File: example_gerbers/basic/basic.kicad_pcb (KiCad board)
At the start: 2 copper layers, 10 x 15 mm, 0 parts

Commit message: Updated basic example
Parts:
- added SP1: Simulation-Port, antmicro-footprints:Simulation-Port, F.Cu at (143.0, 103.3)
- added SP2: Simulation-Port, antmicro-footprints:Simulation-Port, F.Cu at (147.0, 112.6)
- added TP1: Net-Tie_2, antmicro-footprints:NetTie-2_SMD_Pad0.127mm, F.Cu at (143.0, 103.5)
- added TP2: Net-Tie_2, antmicro-footprints:NetTie-2_SMD_Pad0.127mm, B.Cu at (141.0, 114.0)
- added TP3: Net-Tie_2, antmicro-footprints:NetTie-2_SMD_Pad0.127mm, F.Cu at (147.0, 112.4)
- added TP4: Net-Tie_2, antmicro-footprints:NetTie-2_SMD_Pad0.127mm, B.Cu at (141.0, 113.5)
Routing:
- net /MSL: track 0.00 -> 16.1 mm
- net /A: track 14.3 -> 0.00 mm, vias 2 -> 0
- net /B: vias 4 -> 0
- added copper zone on B.Cu, net GND
- removed copper zone on B.Cu, net /B
- removed copper zone on F.Cu, net /B
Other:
- board size 10 x 15 mm -> 9 x 14 mm

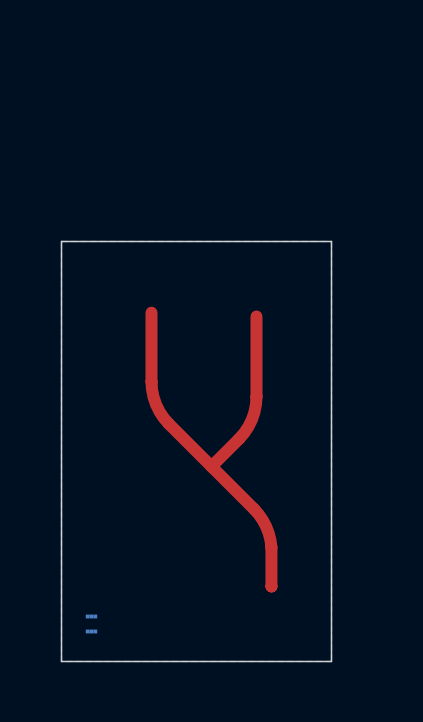
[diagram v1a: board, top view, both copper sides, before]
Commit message: Port position import
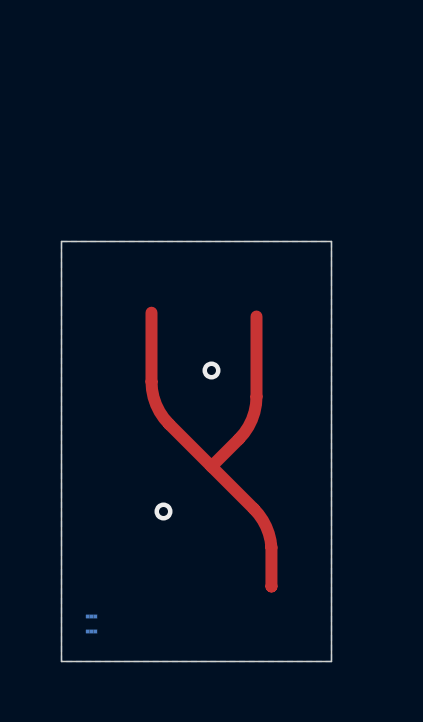
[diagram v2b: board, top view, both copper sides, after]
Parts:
- moved SP2 0.10 mm to (147.0, 112.7)
- moved SP1 0.06 mm to (143.0, 103.2)
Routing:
- net GND: vias 0 -> 2
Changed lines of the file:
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@@
     )
     (pad_to_mask_clearance 0)
+    (aux_axis_origin 140 115)
     (pcbplotparams
       (layerselection 0x00010fc_ffffffff)
@@
       (outputformat 1)
       (mirror false)
-      (drillshape 1)
+      (drillshape 0)
       (scaleselection 1)
       (outputdirectory "")
@@
   )
   (footprint "antmicro-footprints:Simulation-Port" (layer "F.Cu")
-    (at 143 103.3 180)
+    (at 143 103.24 180)
     (attr board_only exclude_from_pos_files exclude_from_bom)
     (fp_text reference "SP1" (at 0 1 180 unlocked) (layer "F.Fab")
       (effects (font (size 1 1) (thickness 0.15)))
     )
-    (fp_text value "Simulation-Port" (at 0 2.5 180 unlocked) (layer "F.Fab")
+    (fp_text value "Simulation-Port" (at 0.1 0.64 180 unlocked) (layer "F.Fab") hide
       (effects (font (size 1 1) (thickness 0.15)))
     )
@@
       (effects (font (size 1 1) (thickness 0.15)))
     )
-    (fp_text user "${REFERENCE}" (at 0 4 180 unlocked) (layer "F.Fab")
+    (fp_text user "${REFERENCE}" (at -3.4 1.6 180 unlocked) (layer "F.Fab") hide
       (effects (font (size 1 1) (thickness 0.15)))
     )
@@
   )
   (footprint "antmicro-footprints:Simulation-Port" (layer "F.Cu")
-    (at 147 112.6)
+    (at 147 112.7)
     (attr board_only exclude_from_pos_files exclude_from_bom)
     (fp_text reference "SP2" (at 0 1 unlocked) (layer "F.Fab")
       (effects (font (size 1 1) (thickness 0.15)))
     )
-    (fp_text value "Simulation-Port" (at 0 2.5 unlocked) (layer "F.Fab")
+    (fp_text value "Simulation-Port" (at 0 1 unlocked) (layer "F.Fab") hide
       (effects (font (size 1 1) (thickness 0.15)))
     )
@@
       (effects (font (size 1 1) (thickness 0.15)))
     )
-    (fp_text user "${REFERENCE}" (at 0 4 unlocked) (layer "F.Fab")
+    (fp_text user "${REFERENCE}" (at 0 2.5 unlocked) (layer "F.Fab") hide
       (effects (font (size 1 1) (thickness 0.15)))
     )
@@
   (arc (start 145.914214 107.585786) (mid 146.34775 106.936938) (end 146.5 106.171573) (width 0.4) (layer "F.Cu") (net 1))
   (arc (start 143 105.671573) (mid 143.15225 106.436939) (end 143.585787 107.085787) (width 0.4) (layer "F.Cu") (net 1))
+  (via (at 145 105.3) (size 0.6) (drill 0.3) (layers "F.Cu" "B.Cu") (free) (net 2))
+  (via (at 143.4 110) (size 0.6) (drill 0.3) (layers "F.Cu" "B.Cu") (free) (net 2))
   (zone (net 2) (net_name "GND") (layer "B.Cu") (hatch edge 0.508)
     (connect_pads yes (clearance 0.2))
